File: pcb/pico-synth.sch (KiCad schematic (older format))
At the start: 44 parts, among them J1 JST XH 2P, J2 JST XH 5P, J3 JST XH 4P, J4 JST XH 3P, SW1 Rotary_Encoder_Switch, U1 Pico, U2 6N137, U3 24LC512, U4 MCP4822, U5 LTC1044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

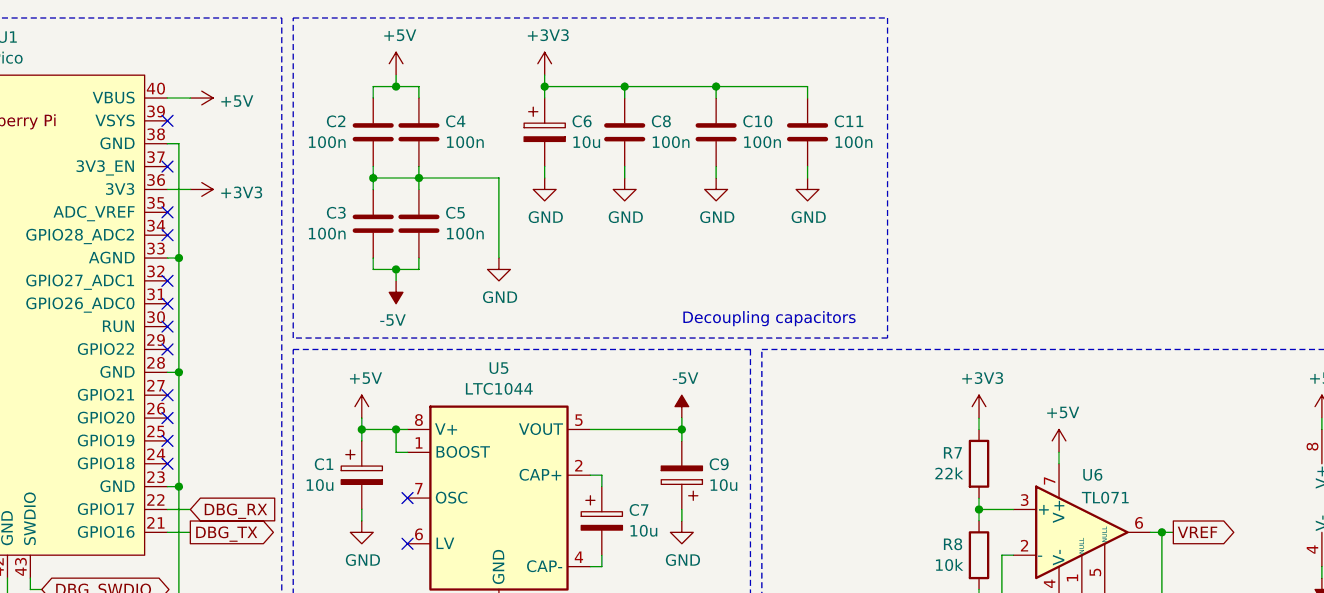
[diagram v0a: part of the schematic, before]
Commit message: new hardware revision: 2.1
this adds a two leds, for output monitoring
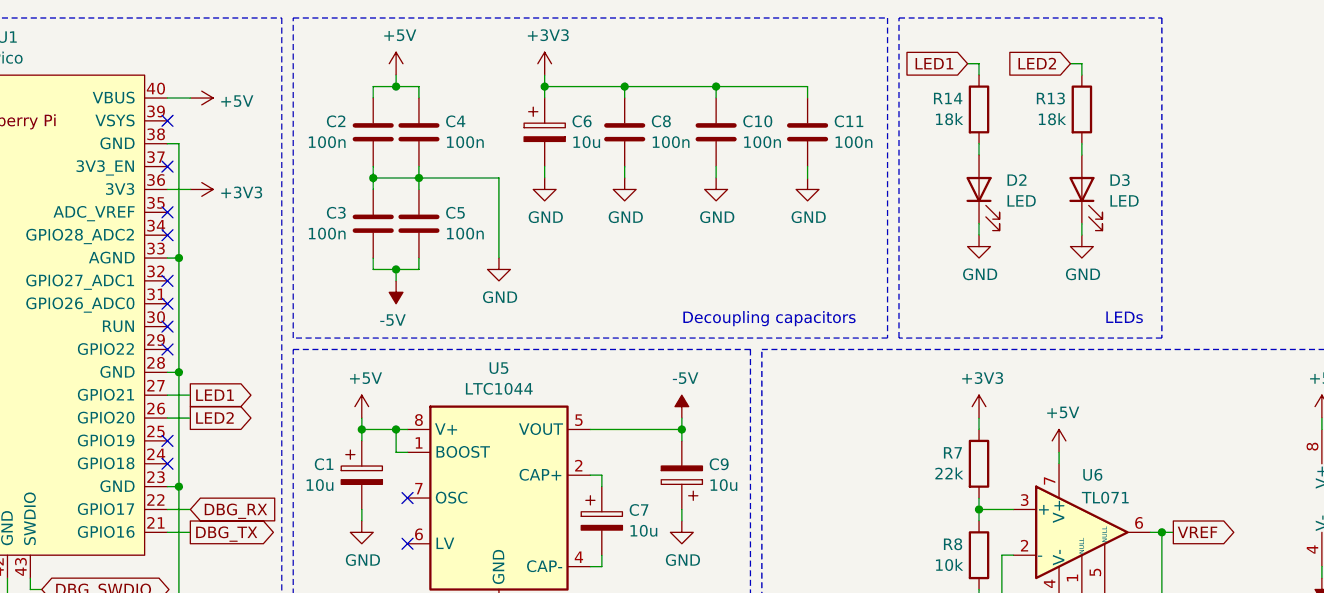
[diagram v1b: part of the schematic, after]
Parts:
- added D2, D3: LED, LED_THT:LED_D3.0mm, symbol Device:LED
- added R13, R14: 18k, Resistor_THT:R_Axial_DIN0207_L6.3mm_D2.5mm_P10.16mm_Horizontal, symbol Device:R
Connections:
- net GND: now also D2.1 (K), D3.1 (K)
- net LED2: now reaches U1.26 (GPIO20)
- net LED2: now also R13.1
- net LED1: now reaches U1.27 (GPIO21)
- net LED1: now also R14.1
- new net: D3.2 (A), R13.2
- new net: D2.2 (A), R14.2
- no-connect marks 24 -> 22
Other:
- note added: "LEDs"
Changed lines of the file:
@@
 Sheet 1 1
 Title "pico-synth"
-Date "2022-01-19"
-Rev "2.0"
+Date "2022-02-01"
+Rev "2.1"
 Comp ""
 Comment1 ""
@@
 NoConn ~ 4050 2950
 NoConn ~ 4050 2850
-NoConn ~ 4050 2750
-NoConn ~ 4050 2650
 NoConn ~ 4050 2450
 NoConn ~ 4050 2350
@@
 Wire Wire Line
 	4050 3250 4150 3250
+$Comp
+L Device:LED D3
+U 1 1 61F9B25F
+P 8050 1750
+F 0 "D3" V 8089 1632 50  0000 R CNN
+F 1 "LED" V 7998 1632 50  0000 R CNN
+F 2 "LED_THT:LED_D3.0mm" H 8050 1750 50  0001 C CNN
+F 3 "~" H 8050 1750 50  0001 C CNN
+	1    8050 1750
+	0    -1   -1   0
+$EndComp
+$Comp
+L power:GND #PWR0101
+U 1 1 61F9C231
+P 8050 1950
+F 0 "#PWR0101" H 8050 1700 50  0001 C CNN
+F 1 "GND" H 8055 1777 50  0000 C CNN
+F 2 "" H 8050 1950 50  0001 C CNN
+F 3 "" H 8050 1950 50  0001 C CNN
+	1    8050 1950
+	1    0    0    -1
+$EndComp
+$Comp
+L Device:LED D2
+U 1 1 61FB2915
+P 7600 1750
+F 0 "D2" V 7639 1632 50  0000 R CNN
+F 1 "LED" V 7548 1632 50  0000 R CNN
+F 2 "LED_THT:LED_D3.0mm" H 7600 1750 50  0001 C CNN
+F 3 "~" H 7600 1750 50  0001 C CNN
+	1    7600 1750
+	0    -1   -1   0
+$EndComp
+$Comp
+L power:GND #PWR0102
+U 1 1 61FB291B
+P 7600 1950
+F 0 "#PWR0102" H 7600 1700 50  0001 C CNN
+F 1 "GND" H 7605 1777 50  0000 C CNN
+F 2 "" H 7600 1950 50  0001 C CNN
+F 3 "" H 7600 1950 50  0001 C CNN
+	1    7600 1950
+	1    0    0    -1
+$EndComp
+$Comp
+L Device:R R13
+U 1 1 61FE7FDF
+P 8050 1400
+F 0 "R13" H 7981 1446 50  0000 R CNN
+F 1 "18k" H 7981 1355 50  0000 R CNN
+F 2 "Resistor_THT:R_Axial_DIN0207_L6.3mm_D2.5mm_P10.16mm_Horizontal" V 7980 1400 50  0001 C CNN
+F 3 "~" H 8050 1400 50  0001 C CNN
+	1    8050 1400
+	1    0    0    -1
+$EndComp
+$Comp
+L Device:R R14
+U 1 1 61FE9F6E
+P 7600 1400
+F 0 "R14" H 7531 1446 50  0000 R CNN
+F 1 "18k" H 7531 1355 50  0000 R CNN
+F 2 "Resistor_THT:R_Axial_DIN0207_L6.3mm_D2.5mm_P10.16mm_Horizontal" V 7530 1400 50  0001 C CNN
+F 3 "~" H 7600 1400 50  0001 C CNN
+	1    7600 1400
+	1    0    0    -1
+$EndComp
+Wire Wire Line
+	8050 1600 8050 1550
+Wire Wire Line
+	7600 1600 7600 1550
+Wire Wire Line
+	8050 1950 8050 1900
+Wire Wire Line
+	7600 1950 7600 1900
+Text GLabel 8000 1200 0    50   Input ~ 0
+LED2
+Text GLabel 7550 1200 0    50   Input ~ 0
+LED1
+Wire Wire Line
+	8000 1200 8050 1200
+Wire Wire Line
+	8050 1200 8050 1250
+Wire Notes Line
+	7250 2400 7250 1000
+Wire Notes Line
+	7250 1000 8400 1000
+Wire Notes Line
+	8400 1000 8400 2400
+Wire Notes Line
+	8400 2400 7250 2400
+Text Notes 8150 2350 0    50   ~ 0
+LEDs
+Wire Wire Line
+	7550 1200 7600 1200
+Wire Wire Line
+	7600 1200 7600 1250
+Text GLabel 4150 2650 2    50   Output ~ 0
+LED1
+Text GLabel 4150 2750 2    50   Output ~ 0
+LED2
+Wire Wire Line
+	4050 2650 4150 2650
+Wire Wire Line
+	4050 2750 4150 2750
 $EndSCHEMATC
